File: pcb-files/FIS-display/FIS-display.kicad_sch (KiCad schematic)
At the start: 31 parts, among them J1 Conn_01x03_Pin, J2 Conn_01x03_Socket, J3 Conn_01x02_Socket, Q1 BS170, Q2 BS170, Q3 BS170, Q4 BS170, Q5 BS170, Q6 BS170, U2 MCP2561-H-P

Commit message: PCB: update KiCad design and Gerbers; add design backups
Made-with: Cursor
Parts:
- removed J2: Conn_01x03_Socket, Connector_JST:JST_PH_B3B-PH-K_1x03_P2.00mm_Vertical, symbol Connector:Conn_01x03_Socket
- added J2: Conn_01x03_Pin, Connector_PinHeader_2.54mm:PinHeader_1x03_P2.54mm_Vertical, symbol Connector:Conn_01x03_Pin
- J1: footprint Connector_JST:JST_PH_B3B-PH-K_1x03_P2.00mm_Vertical -> Connector_PinHeader_2.54mm:PinHeader_1x03_P2.54mm_Vertical
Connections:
- net RX_CLK: now also J2.2 (Pin_2)
- net RX_DATA: now also J2.3 (Pin_3)
- net RX_ENA: now also J2.1 (Pin_1)
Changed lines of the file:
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@@
 	(text "3LB RX "
 		(exclude_from_sim no)
-		(at 38.354 157.988 0)
+		(at 37.846 156.972 0)
 		(effects
 			(font
@@
 	(text "3LB TX"
 		(exclude_from_sim no)
-		(at 39.878 134.62 0)
+		(at 39.116 136.652 0)
 		(effects
 			(font
@@
 	)
 	(symbol
-		(lib_id "Connector:Conn_01x03_Socket")
-		(at 27.94 163.83 0)
-		(mirror y)
-		(unit 1)
-		(exclude_from_sim no)
-		(in_bom yes)
-		(on_board yes)
-		(dnp no)
-		(property "Reference" "J2"
-			(at 28.575 171.45 0)
-			(effects
-				(font
-					(size 1.27 1.27)
-				)
-			)
-		)
-		(property "Value" "Conn_01x03_Socket"
-			(at 28.575 168.91 0)
-			(effects
-				(font
-					(size 1.27 1.27)
-				)
-			)
-		)
-		(property "Footprint" "Connector_JST:JST_PH_B3B-PH-K_1x03_P2.00mm_Vertical"
-			(at 27.94 163.83 0)
-			(effects
-				(font
-					(size 1.27 1.27)
-				)
-				(hide yes)
-			)
-		)
-		(property "Datasheet" "~"
-			(at 27.94 163.83 0)
-			(effects
-				(font
-					(size 1.27 1.27)
-				)
-				(hide yes)
-			)
-		)
-		(property "Description" "Generic connector, single row, 01x03, script generated"
-			(at 27.94 163.83 0)
-			(effects
-				(font
-					(size 1.27 1.27)
-				)
-				(hide yes)
-			)
-		)
-		(pin "3"
-		)
-		(pin "2"
-		)
-		(pin "1"
-		)
-		(instances
-			(project ""
-				(path "/5f5d06d6-8a1b-4149-9ddf-636ba9f7cf70"
-					(reference "J2")
-					(unit 1)
-				)
-			)
-		)
-	)
-	(symbol
 		(lib_id "Device:R")
 		(at 132.08 100.33 0)
@@
 	)
 	(symbol
-		(lib_id "Connector:Conn_01x03_Pin")
-		(at 29.21 143.51 0)
-		(unit 1)
-		(exclude_from_sim no)
-		(in_bom yes)
-		(on_board yes)
-		(dnp no)
-		(property "Reference" "J1"
-			(at 31.496 149.86 0)
-			(effects
-				(font
-					(size 1.27 1.27)
-				)
-			)
-		)
-		(property "Value" "Conn_01x03_Pin"
-			(at 31.496 147.828 0)
-			(effects
-				(font
-					(size 1.27 1.27)
-				)
-			)
-		)
-		(property "Footprint" "Connector_JST:JST_PH_B3B-PH-K_1x03_P2.00mm_Vertical"
-			(at 29.21 143.51 0)
-			(effects
-				(font
-					(size 1.27 1.27)
-				)
-				(hide yes)
-			)
-		)
-		(property "Datasheet" "~"
-			(at 29.21 143.51 0)
-			(effects
-				(font
-					(size 1.27 1.27)
-				)
-				(hide yes)
-			)
-		)
-		(property "Description" "Generic connector, single row, 01x03, script generated"
-			(at 29.21 143.51 0)
-			(effects
-				(font
-					(size 1.27 1.27)
-				)
-				(hide yes)
-			)
-		)
-		(pin "1"
-		)
-		(pin "2"
-		)
-		(pin "3"
-		)
-		(instances
-			(project ""
-				(path "/5f5d06d6-8a1b-4149-9ddf-636ba9f7cf70"
-					(reference "J1")
-					(unit 1)
-				)
-			)
-		)
-	)
-	(symbol
 		(lib_id "Transistor_FET:BS170")
 		(at 57.15 102.87 270)
@@
 	)
 	(symbol
+		(lib_id "Connector:Conn_01x03_Pin")
+		(at 29.21 143.51 0)
+		(unit 1)
+		(exclude_from_sim no)
+		(in_bom yes)
+		(on_board yes)
+		(dnp no)
+		(fields_autoplaced yes)
+		(property "Reference" "J1"
+			(at 29.845 135.89 0)
+			(effects
+				(font
+					(size 1.27 1.27)
+				)
+			)
+		)
+		(property "Value" "Conn_01x03_Pin"
+			(at 29.845 138.43 0)
+			(effects
+				(font
+					(size 1.27 1.27)
+				)
+			)
+		)
+		(property "Footprint" "Connector_PinHeader_2.54mm:PinHeader_1x03_P2.54mm_Vertical"
+			(at 29.21 143.51 0)
+			(effects
+				(font
+					(size 1.27 1.27)
+				)
+				(hide yes)
+			)
+		)
+		(property "Datasheet" "~"
+			(at 29.21 143.51 0)
+			(effects
+				(font
+					(size 1.27 1.27)
+				)
+				(hide yes)
+			)
+		)
+		(property "Description" "Generic connector, single row, 01x03, script generated"
+			(at 29.21 143.51 0)
+			(effects
+				(font
+					(size 1.27 1.27)
+				)
+				(hide yes)
+			)
+		)
+		(pin "3"
+		)
+		(pin "1"
+		)
+		(pin "2"
+		)
+		(instances
+			(project ""
+				(path "/5f5d06d6-8a1b-4149-9ddf-636ba9f7cf70"
+					(reference "J1")
+					(unit 1)
+				)
+			)
+		)
+	)
+	(symbol
 		(lib_id "power:GND")
 		(at 83.82 170.18 0)
@@
 					(unit 1)
 				)
+			)
+		)
+	)
+	(symbol
+		(lib_id "Connector:Conn_01x03_Pin")
+		(at 27.94 163.83 0)
+		(unit 1)
+		(exclude_from_sim no)
+		(in_bom yes)
+		(on_board yes)
+		(dnp no)
+		(fields_autoplaced yes)
+		(property "Reference" "J2"
+			(at 28.575 156.21 0)
+			(effects
+				(font
+					(size 1.27 1.27)
+				)
+			)
+		)
+		(property "Value" "Conn_01x03_Pin"
+			(at 28.575 158.75 0)
+			(effects
+				(font
+					(size 1.27 1.27)
+				)
+			)
+		)
+		(property "Footprint" "Connector_PinHeader_2.54mm:PinHeader_1x03_P2.54mm_Vertical"
+			(at 27.94 163.83 0)
+			(effects
+				(font
+					(size 1.27 1.27)
+				)
+				(hide yes)
+			)
+		)
+		(property "Datasheet" "~"
+			(at 27.94 163.83 0)
+			(effects
+				(font
+					(size 1.27 1.27)
+				)
+				(hide yes)
+			)
+		)
+		(property "Description" "Generic connector, single row, 01x03, script generated"
+			(at 27.94 163.83 0)
+			(effects
+				(font
+					(size 1.27 1.27)
+				)
+				(hide yes)
+			)
+		)
+		(pin "3"
+		)
+		(pin "2"
+		)
+		(pin "1"
+		)
+		(instances
+			(project ""
+				(path "/5f5d06d6-8a1b-4149-9ddf-636ba9f7cf70"
+					(reference "J2")
+					(unit 1)
+				)

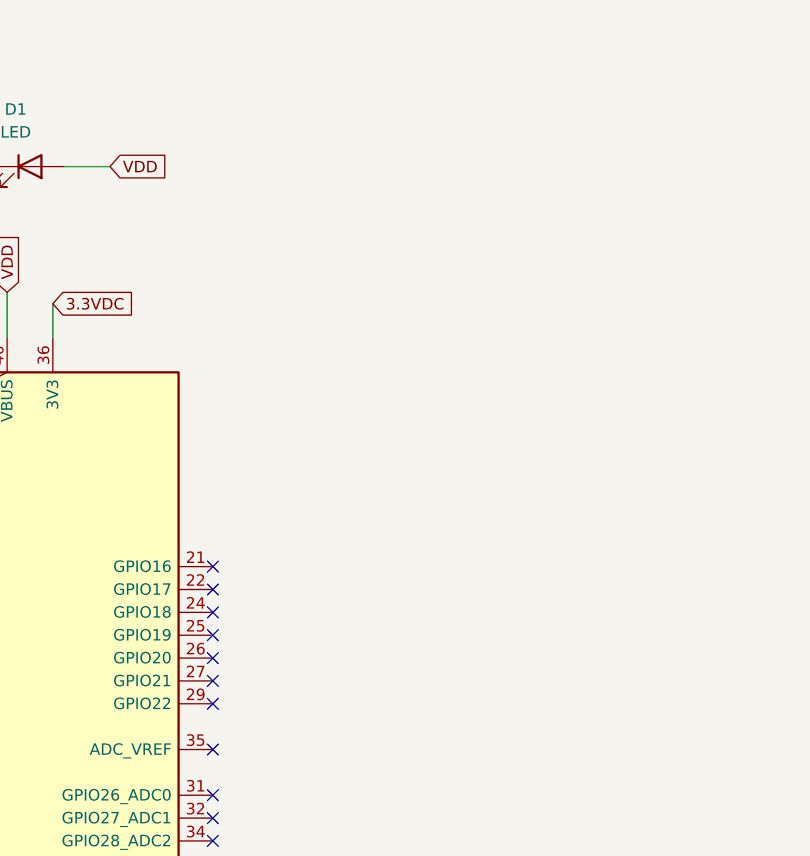
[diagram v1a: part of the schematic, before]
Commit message: README: add PCB 3D image; update PCB/KiCad and Gerbers
Made-with: Cursor
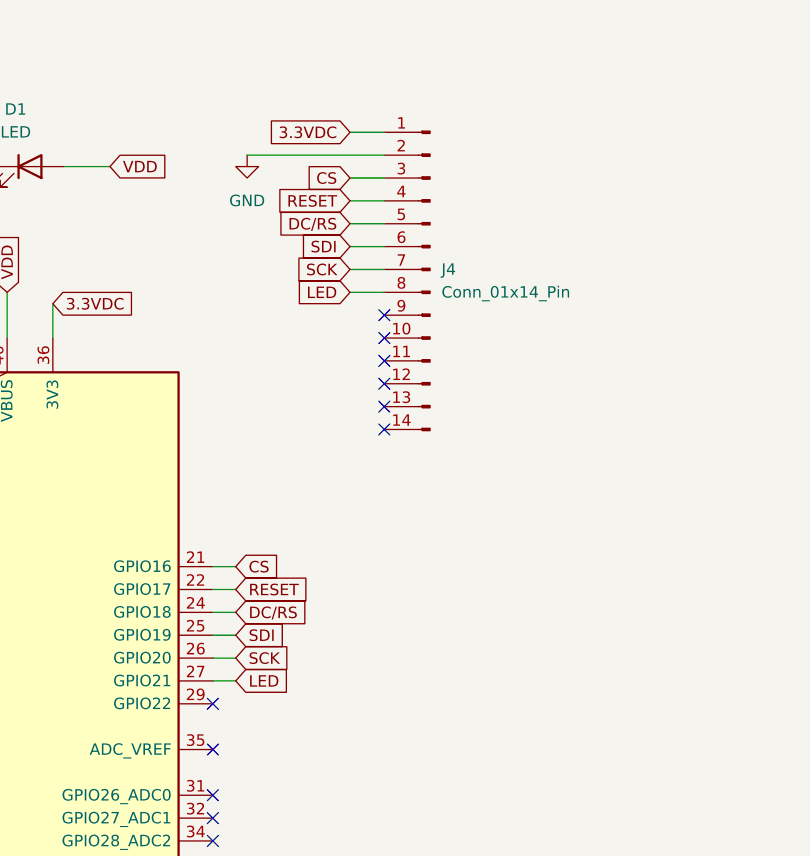
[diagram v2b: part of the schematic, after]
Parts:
- added J4: Conn_01x14_Pin, Connector_PinHeader_2.54mm:PinHeader_1x14_P2.54mm_Vertical, symbol Connector:Conn_01x14_Pin
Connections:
- net 3.3VDC: now also J4.1 (Pin_1)
- net GND: now also J4.2 (Pin_2)
- net CS: now reaches A1.21 (GPIO16)
- net CS: now also J4.3 (Pin_3)
- net RESET: now reaches A1.22 (GPIO17)
- net RESET: now also J4.4 (Pin_4)
- net DC/RS: now reaches A1.24 (GPIO18)
- net DC/RS: now also J4.5 (Pin_5)
- net SDI: now reaches A1.25 (GPIO19)
- net SDI: now also J4.6 (Pin_6)
- net SCK: now reaches A1.26 (GPIO20)
- net SCK: now also J4.7 (Pin_7)
- net LED: now reaches A1.27 (GPIO21)
- net LED: now also J4.8 (Pin_8)

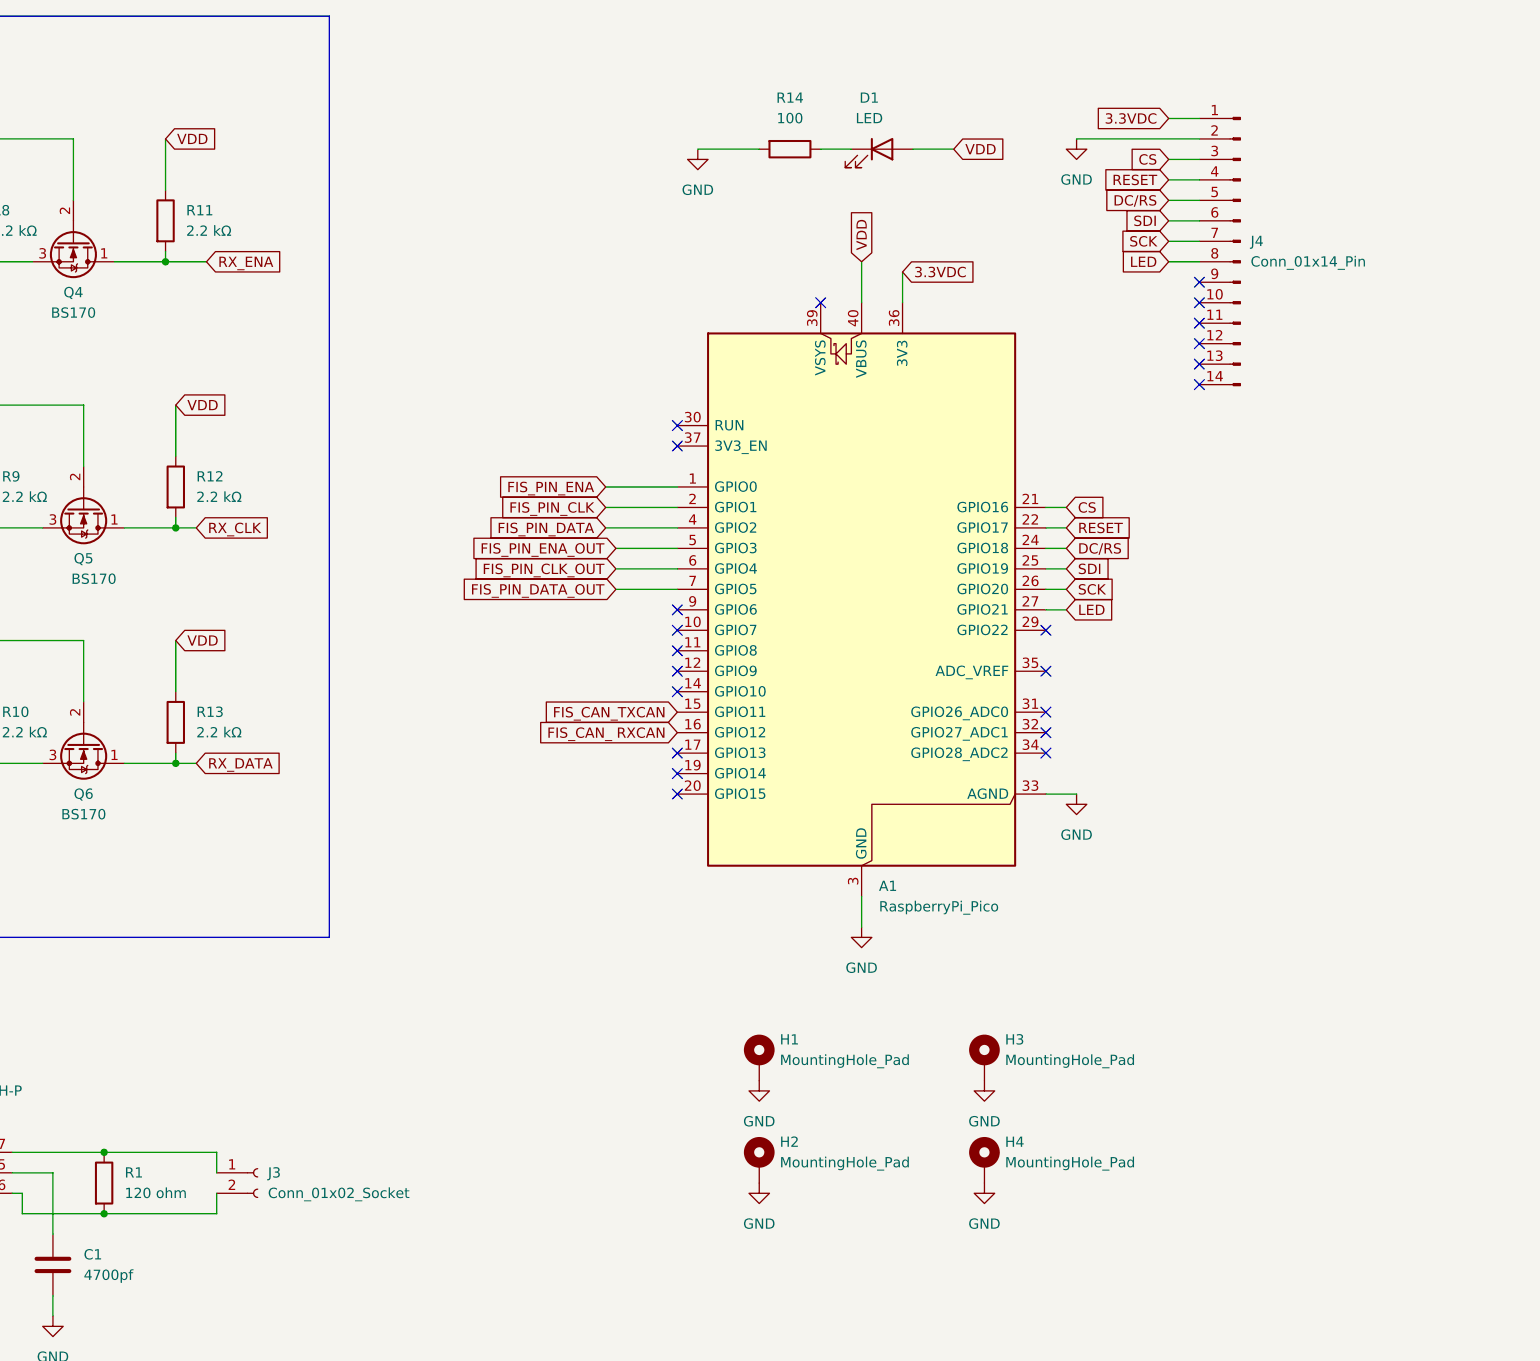
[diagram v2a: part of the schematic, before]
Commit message: README: section 10 formatting, LCD wiki/driver refs, ILI9341 window addressing; PCB/KiCad/PDF/Gerbers
Made-with: Cursor
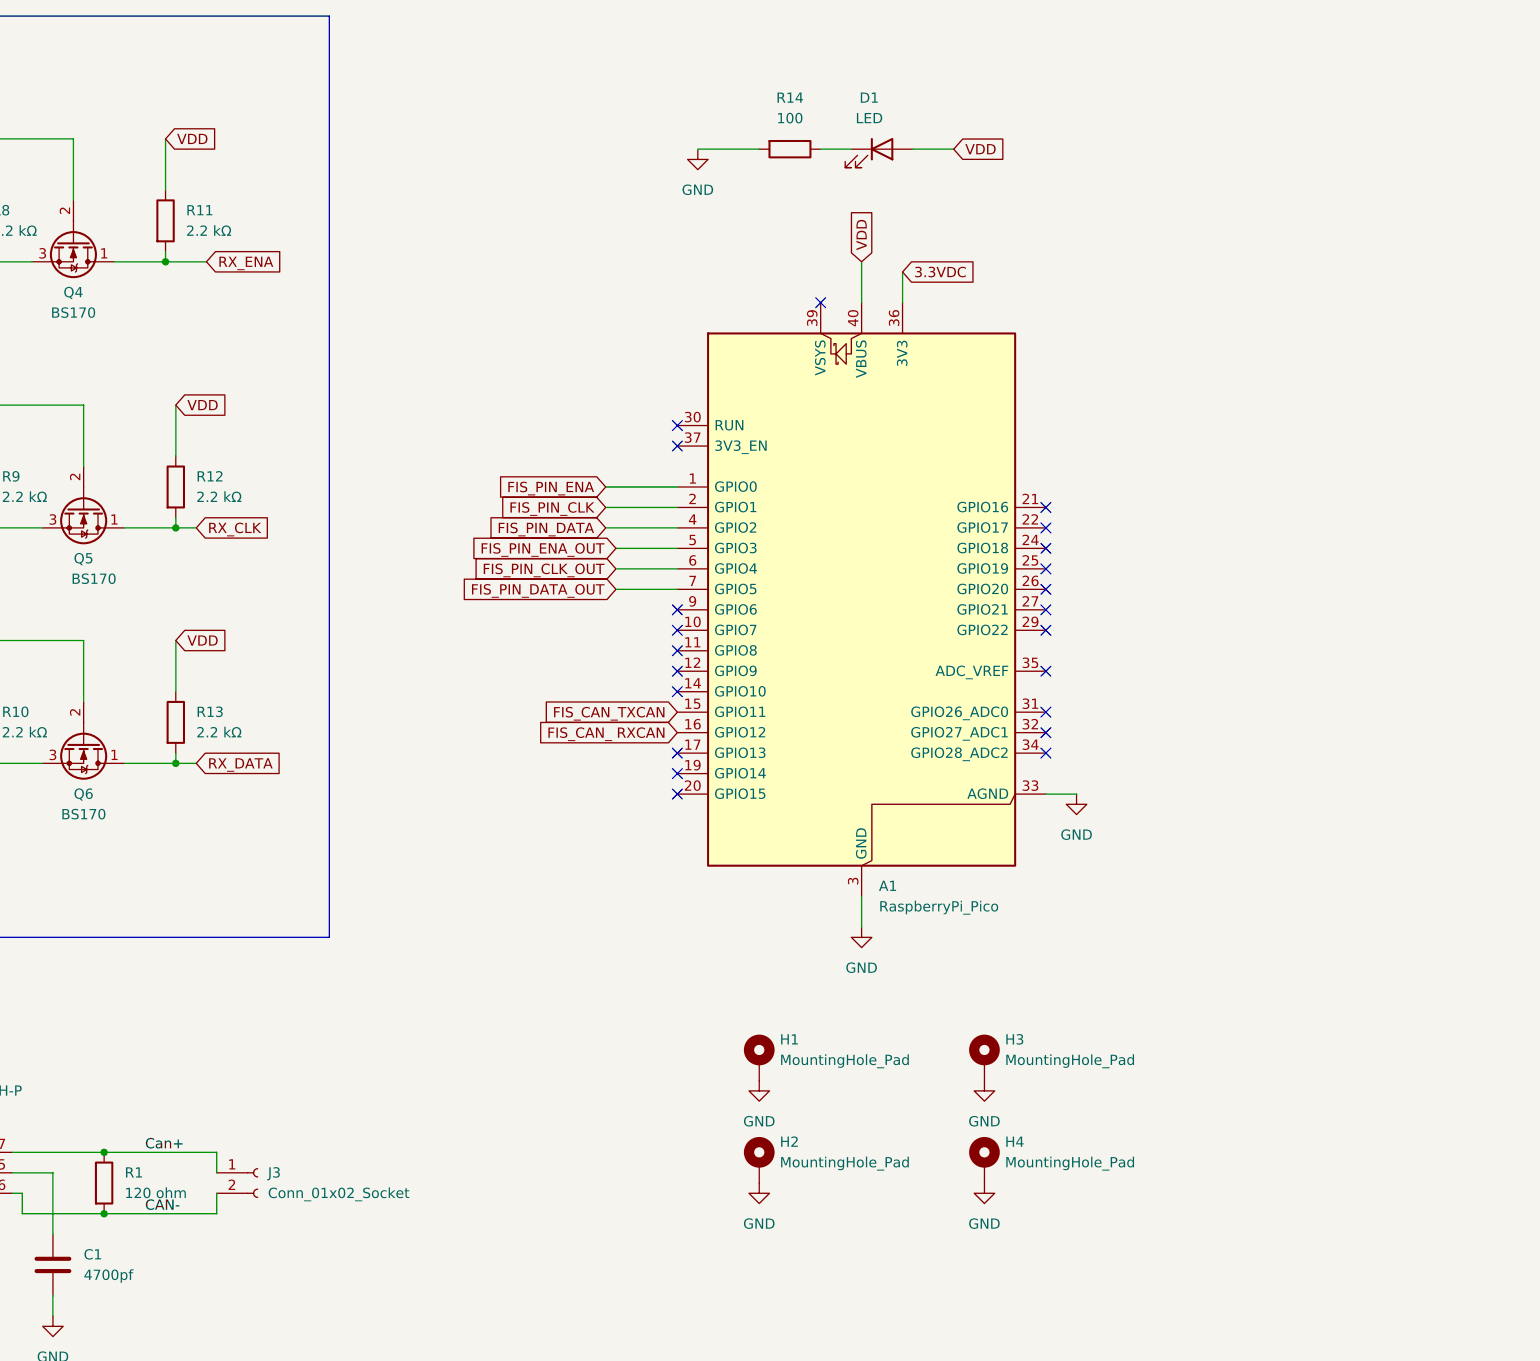
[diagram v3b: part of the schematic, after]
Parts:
- removed J4: Conn_01x14_Pin, Connector_PinHeader_2.54mm:PinHeader_1x14_P2.54mm_Vertical, symbol Connector:Conn_01x14_Pin
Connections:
- net CAN-: now reaches J3.2 (Pin_2), R1.2, U2.6 (CANL)
- net Can+: now reaches J3.1 (Pin_1), R1.1, U2.7 (CANH)
- net CS: no longer names the net of A1.21 (GPIO16)
- net DC/RS: no longer names the net of A1.24 (GPIO18)
- net LED: no longer names the net of A1.27 (GPIO21)
- net RESET: no longer names the net of A1.22 (GPIO17)
- net SCK: no longer names the net of A1.26 (GPIO20)
- net SDI: no longer names the net of A1.25 (GPIO19)
